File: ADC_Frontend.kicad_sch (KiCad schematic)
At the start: 22 parts, among them U5 THS4551

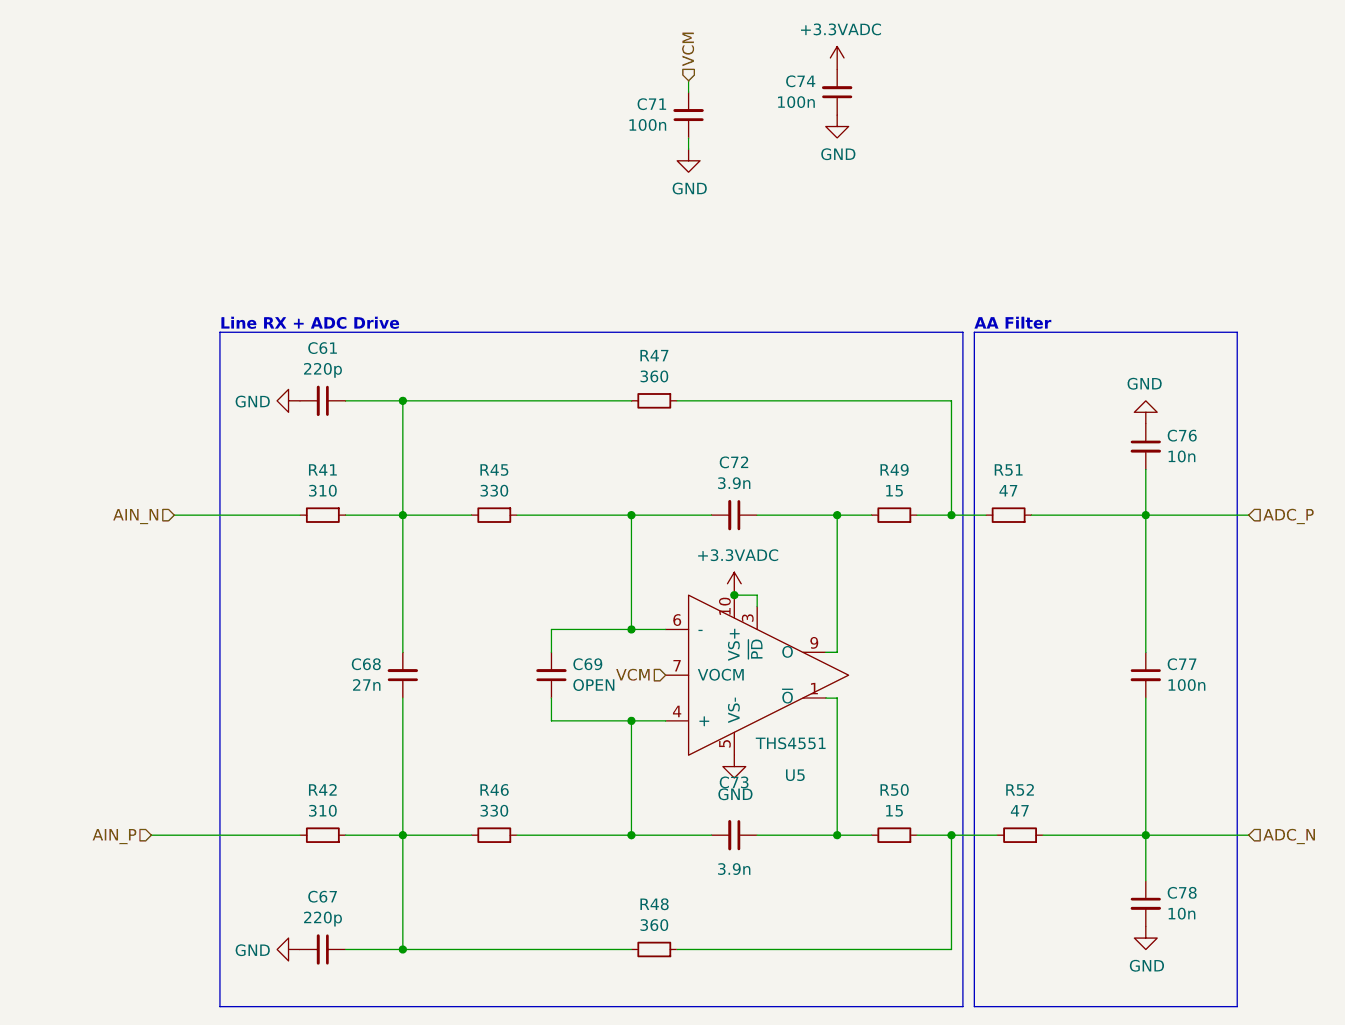
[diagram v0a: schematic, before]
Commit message: (deps) upgrade to KiCad 7.0
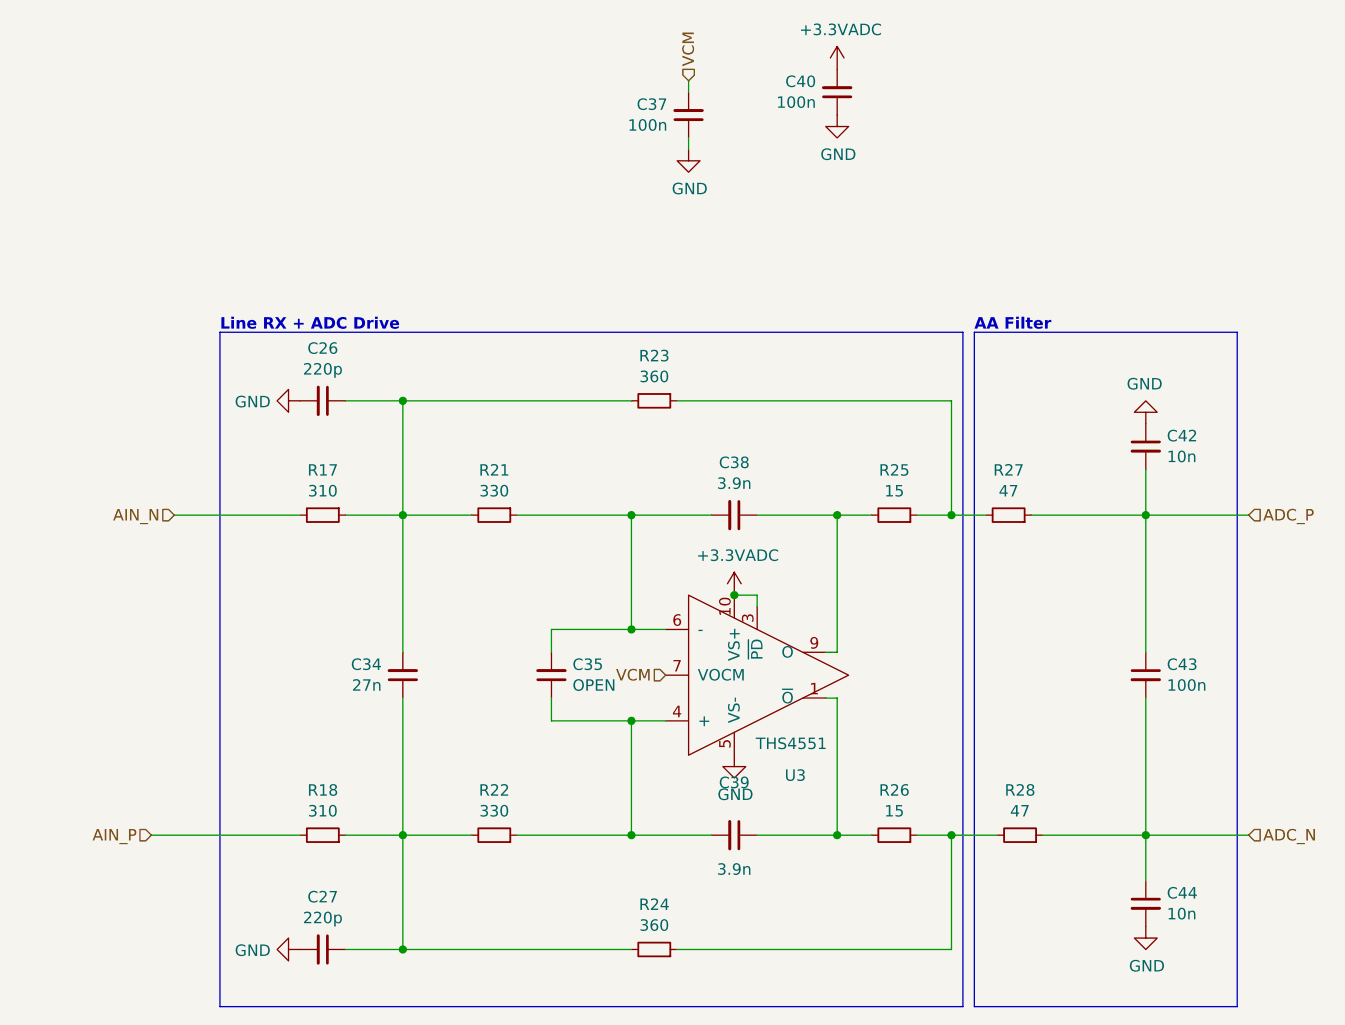
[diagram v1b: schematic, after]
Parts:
- renumbered C61 to C26, C67 to C27, C68 to C34, C69 to C35, C71 to C37, C72 to C38, C73 to C39, C74 to C40, C76 to C42, C77 to C43, C78 to C44, R41 to R17, R42 to R18, R45 to R21, R46 to R22, R47 to R23, R48 to R24, R49 to R25, R50 to R26, R51 to R27, R52 to R28, U5 to U3

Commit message: (sch) relabel
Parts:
- renumbered C26 to C701, C27 to C702, C34 to C703, C35 to C704, C37 to C705, C38 to C706, C39 to C707, C40 to C708, C42 to C709, C43 to C710, C44 to C711, R17 to R701, R18 to R702, R21 to R703, R22 to R704, R23 to R705, R24 to R706, R25 to R707, R26 to R708, R27 to R709, R28 to R710, U3 to U701

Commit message: (sch) change 2.2k R to 0402
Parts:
- R709, R710: footprint Resistor_SMD:R_0603_1608Metric_Pad0.98x0.95mm_HandSolder -> Resistor_SMD:R_0402_1005Metric; MPN ERJ-3EKF47R0V -> RT0402FRE0747RL; Mfr. Panasonic -> Yageo
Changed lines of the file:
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@@
       (effects (font (size 1.27 1.27)))
     )
-    (property "Footprint" "Resistor_SMD:R_0603_1608Metric_Pad0.98x0.95mm_HandSolder" (at 162.56 101.6 0)
+    (property "Footprint" "Resistor_SMD:R_0402_1005Metric" (at 162.56 101.6 0)
       (effects (font (size 1.27 1.27)) hide)
     )
@@
       (effects (font (size 1.27 1.27)) hide)
     )
-    (property "MPN" "ERJ-3EKF47R0V" (at 162.56 101.6 0)
-      (effects (font (size 1.27 1.27)) hide)
-    )
-    (property "Mfr." "Panasonic" (at 162.56 101.6 0)
+    (property "MPN" "RT0402FRE0747RL" (at 162.56 101.6 0)
+      (effects (font (size 1.27 1.27)) hide)
+    )
+    (property "Mfr." "Yageo" (at 162.56 101.6 0)
       (effects (font (size 1.27 1.27)) hide)
     )
@@
         (path "/4185c36c-c66e-4dbd-be5d-841e551f4885/00000000-0000-0000-0000-00005ee5ecad/00000000-0000-0000-0000-00005ee91c90"
           (reference "R809") (unit 1)
-        )
-      )
-    )
-  )
-  (symbol (lib_id "Device:R_Small") (at 163.83 137.16 270) (mirror x) (unit 1)
-    (in_bom yes) (on_board yes) (dnp no)
-    (property "Reference" "R710" (at 163.83 132.1816 90)
-      (effects (font (size 1.27 1.27)))
-    )
-    (property "Value" "47" (at 163.83 134.493 90)
-      (effects (font (size 1.27 1.27)))
-    )
-    (property "Footprint" "Resistor_SMD:R_0603_1608Metric_Pad0.98x0.95mm_HandSolder" (at 163.83 137.16 0)
-      (effects (font (size 1.27 1.27)) hide)
-    )
-    (property "Datasheet" "~" (at 163.83 137.16 0)
-      (effects (font (size 1.27 1.27)) hide)
-    )
-    (property "MPN" "ERJ-3EKF47R0V" (at 163.83 137.16 0)
-      (effects (font (size 1.27 1.27)) hide)
-    )
-    (property "Mfr." "Panasonic" (at 163.83 137.16 0)
-      (effects (font (size 1.27 1.27)) hide)
-    )
-    (pin "1")
-    (pin "2")
-    (instances
-      (project "kleinvoet"
-        (path "/4185c36c-c66e-4dbd-be5d-841e551f4885/00000000-0000-0000-0000-00005ee5ecad/00000000-0000-0000-0000-00005ee62baf"
-          (reference "R710") (unit 1)
-        )
-        (path "/4185c36c-c66e-4dbd-be5d-841e551f4885/00000000-0000-0000-0000-00005ee5ecad/00000000-0000-0000-0000-00005ee91c90"
-          (reference "R810") (unit 1)
         )
       )
@@
         )
       )
+    )
+  )
+  (symbol (lib_id "Device:R_Small") (at 163.83 137.16 270) (mirror x) (unit 1)
+    (in_bom yes) (on_board yes) (dnp no)
+    (property "Reference" "R710" (at 163.83 132.1816 90)
+      (effects (font (size 1.27 1.27)))
+    )
+    (property "Value" "47" (at 163.83 134.493 90)
+      (effects (font (size 1.27 1.27)))
+    )
+    (property "Footprint" "Resistor_SMD:R_0402_1005Metric" (at 163.83 137.16 0)
+      (effects (font (size 1.27 1.27)) hide)
+    )
+    (property "Datasheet" "~" (at 163.83 137.16 0)
+      (effects (font (size 1.27 1.27)) hide)
+    )
+    (property "MPN" "RT0402FRE0747RL" (at 163.83 137.16 0)
+      (effects (font (size 1.27 1.27)) hide)
+    )
+    (property "Mfr." "Yageo" (at 163.83 137.16 0)
+      (effects (font (size 1.27 1.27)) hide)
+    )
+    (pin "1")
+    (pin "2")
+    (instances
+      (project "kleinvoet"
+        (path "/4185c36c-c66e-4dbd-be5d-841e551f4885/00000000-0000-0000-0000-00005ee5ecad/00000000-0000-0000-0000-00005ee62baf"
+          (reference "R710") (unit 1)
+        )
+        (path "/4185c36c-c66e-4dbd-be5d-841e551f4885/00000000-0000-0000-0000-00005ee5ecad/00000000-0000-0000-0000-00005ee91c90"
+          (reference "R810") (unit 1)
+        )
+      )

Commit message: (sch) change passives to 0402
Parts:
- C701, C702: footprint Capacitor_SMD:C_0603_1608Metric_Pad1.08x0.95mm_HandSolder -> Capacitor_SMD:C_0402_1005Metric; MPN C0603C221J5GACTU -> GRT1555C1H221FA02D; Mfr. KEMET -> Murata
- C703: footprint Capacitor_SMD:C_0603_1608Metric_Pad1.08x0.95mm_HandSolder -> Capacitor_SMD:C_0402_1005Metric; MPN CC0603JRX7R9BB273 -> GRM1555C1H272GE01D; Mfr. Yageo -> Murata
- C706, C707: footprint Capacitor_SMD:C_0603_1608Metric_Pad1.08x0.95mm_HandSolder -> Capacitor_SMD:C_0402_1005Metric; MPN CC0603JRX7R9BB392 -> GRM1555C1H392GE01D; Mfr. Yageo -> Murata
- C709, C711: footprint Capacitor_SMD:C_0603_1608Metric_Pad1.08x0.95mm_HandSolder -> Capacitor_SMD:C_0603_1608Metric; MPN C0603C103J5RACTU -> GRM1885C1H103JA01J; Mfr. KEMET -> Murata
- R701, R702: value 310 -> 310E; footprint Resistor_SMD:R_0603_1608Metric_Pad0.98x0.95mm_HandSolder -> Resistor_SMD:R_0402_1005Metric; MPN ERJ-3EKF3090V -> RT0402FRE07309RL; Mfr. Panasonic -> Yageo
- R703, R704: value 330 -> 330E; footprint Resistor_SMD:R_0603_1608Metric_Pad0.98x0.95mm_HandSolder -> Resistor_SMD:R_0402_1005Metric; MPN ERJ-3EKF3300V -> RT0402FRE07330RL; Mfr. Panasonic -> Yageo
- R705, R706: value 360 -> 360E; footprint Resistor_SMD:R_0603_1608Metric_Pad0.98x0.95mm_HandSolder -> Resistor_SMD:R_0402_1005Metric; MPN ERJ-3EKF3600V -> RT0402FRE07360RL; Mfr. Panasonic -> Yageo
- R707, R708: value 15 -> 14.7E; footprint Resistor_SMD:R_0603_1608Metric_Pad0.98x0.95mm_HandSolder -> Resistor_SMD:R_0402_1005Metric; MPN ERJ-3EKF15R0V -> RT0603FRE0714R7L; Mfr. Panasonic -> Yageo
- R709, R710: value 47 -> 47E

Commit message: (pcb) initial layout
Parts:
- C704: footprint Capacitor_SMD:C_0603_1608Metric_Pad1.08x0.95mm_HandSolder -> Capacitor_SMD:C_0402_1005Metric
- C705, C708, C710: footprint Capacitor_SMD:C_0603_1608Metric_Pad1.08x0.95mm_HandSolder -> Capacitor_SMD:C_0402_1005Metric; MPN C0603C104M5RACTU -> C0402C104K8PACTU
- C709, C711: footprint Capacitor_SMD:C_0603_1608Metric -> Capacitor_SMD:C_0402_1005Metric; MPN GRM1885C1H103JA01J -> (none)
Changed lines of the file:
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@@
       (effects (font (size 1.27 1.27)) (justify right))
     )
-    (property "Footprint" "Capacitor_SMD:C_0603_1608Metric_Pad1.08x0.95mm_HandSolder" (at 111.76 119.38 0)
+    (property "Footprint" "Capacitor_SMD:C_0402_1005Metric" (at 111.76 119.38 0)
       (effects (font (size 1.27 1.27)) hide)
     )
@@
       (effects (font (size 1.27 1.27)) (justify left))
     )
-    (property "Footprint" "Capacitor_SMD:C_0603_1608Metric_Pad1.08x0.95mm_HandSolder" (at 177.8 119.38 0)
+    (property "Footprint" "Capacitor_SMD:C_0402_1005Metric" (at 177.8 119.38 0)
       (effects (font (size 1.27 1.27)) hide)
     )
@@
       (effects (font (size 1.27 1.27)) hide)
     )
-    (property "MPN" "C0603C104M5RACTU" (at 177.8 119.38 0)
+    (property "MPN" "C0402C104K8PACTU" (at 177.8 119.38 0)
       (effects (font (size 1.27 1.27)) hide)
     )
@@
       (effects (font (size 1.27 1.27)) (justify left))
     )
-    (property "Footprint" "Capacitor_SMD:C_0603_1608Metric" (at 177.8 93.98 0)
+    (property "Footprint" "Capacitor_SMD:C_0402_1005Metric" (at 177.8 93.98 0)
       (effects (font (size 1.27 1.27)) hide)
     )
@@
       (effects (font (size 1.27 1.27)) hide)
     )
-    (property "MPN" "GRM1885C1H103JA01J" (at 177.8 93.98 0)
+    (property "MPN" "" (at 177.8 93.98 0)
       (effects (font (size 1.27 1.27)) hide)
     )
@@
       (effects (font (size 1.27 1.27)) (justify left))
     )
-    (property "Footprint" "Capacitor_SMD:C_0603_1608Metric" (at 177.8 144.78 0)
+    (property "Footprint" "Capacitor_SMD:C_0402_1005Metric" (at 177.8 144.78 0)
       (effects (font (size 1.27 1.27)) hide)
     )
@@
       (effects (font (size 1.27 1.27)) hide)
     )
-    (property "MPN" "GRM1885C1H103JA01J" (at 177.8 144.78 0)
+    (property "MPN" "" (at 177.8 144.78 0)
       (effects (font (size 1.27 1.27)) hide)
     )
@@
       (effects (font (size 1.27 1.27)) (justify right))
     )
-    (property "Footprint" "Capacitor_SMD:C_0603_1608Metric_Pad1.08x0.95mm_HandSolder" (at 127 57.15 0)
+    (property "Footprint" "Capacitor_SMD:C_0402_1005Metric" (at 127 57.15 0)
       (effects (font (size 1.27 1.27)) hide)
     )
@@
       (effects (font (size 1.27 1.27)) hide)
     )
-    (property "MPN" "C0603C104M5RACTU" (at 127 57.15 0)
+    (property "MPN" "C0402C104K8PACTU" (at 127 57.15 0)
       (effects (font (size 1.27 1.27)) hide)
     )
@@
       (effects (font (size 1.27 1.27)) (justify right))
     )
-    (property "Footprint" "Capacitor_SMD:C_0603_1608Metric_Pad1.08x0.95mm_HandSolder" (at 143.51 54.61 0)
+    (property "Footprint" "Capacitor_SMD:C_0402_1005Metric" (at 143.51 54.61 0)
       (effects (font (size 1.27 1.27)) hide)
     )
@@
       (effects (font (size 1.27 1.27)) hide)
     )
-    (property "MPN" "C0603C104M5RACTU" (at 143.51 54.61 0)
-      (effects (font (size 1.27 1.27)) hide)
-    )
+    (property "MPN" "C0402C104K8PACTU" (at 143.51 54.61 0)
+      (effects (font (size 1.27 1.27)) hide)
+    )

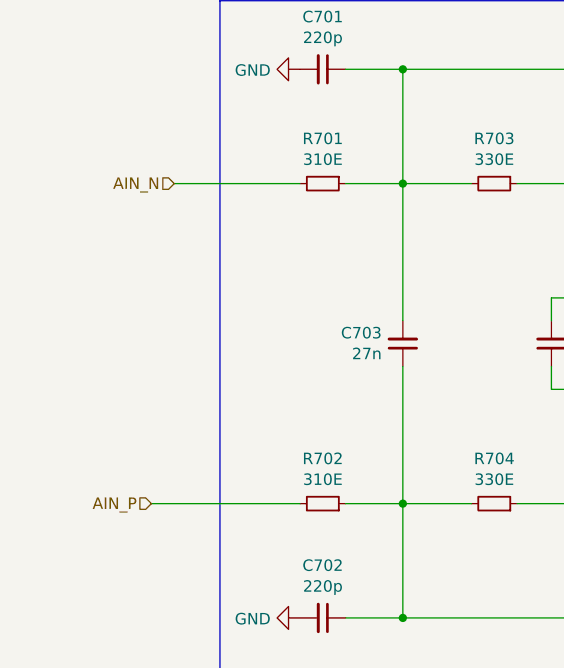
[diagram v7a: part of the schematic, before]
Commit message: (sch) add net labels
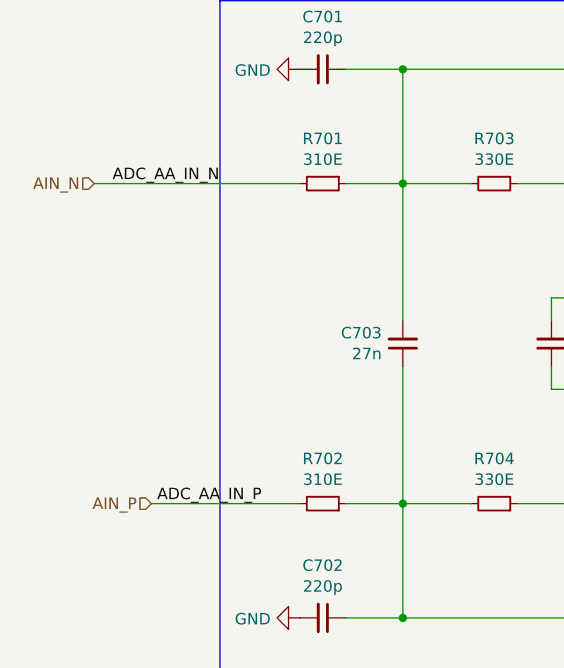
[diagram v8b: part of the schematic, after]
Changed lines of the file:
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@@
+    (stroke (width 0) (type default))
+  )
+  (wire (pts (xy 60.96 101.6) (xy 83.82 101.6))
     (stroke (width 0) (type default))
   )
@@
   )
   (wire (pts (xy 152.4 137.16) (xy 156.21 137.16))
-    (stroke (width 0) (type default))
-  )
-  (wire (pts (xy 69.85 101.6) (xy 83.82 101.6))
     (stroke (width 0) (type default))
   )
@@
     (effects (font (size 1.27 1.27) (thickness 0.254) bold) (justify left bottom))
   )
+  (label "ADC_AA_IN_P" (at 67.945 137.16 0) (fields_autoplaced)
+    (effects (font (size 1.27 1.27)) (justify left bottom))
+  )
+  (label "ADC_AA_IN_N" (at 62.992 101.6 0) (fields_autoplaced)
+    (effects (font (size 1.27 1.27)) (justify left bottom))
+  )
   (hierarchical_label "ADC_P" (shape input) (at 189.23 101.6 0) (fields_autoplaced)
     (effects (font (size 1.27 1.27)) (justify left))
   )
-  (hierarchical_label "AIN_N" (shape input) (at 69.85 101.6 180) (fields_autoplaced)
+  (hierarchical_label "AIN_N" (shape input) (at 60.96 101.6 180) (fields_autoplaced)
     (effects (font (size 1.27 1.27)) (justify right))
   )
